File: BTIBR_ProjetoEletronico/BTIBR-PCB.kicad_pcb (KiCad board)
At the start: 2 copper layers, 100 x 100 mm, 63 parts, among them J1 Screw_Terminal_01x04, J10 Conn_01x03_Male, J11 Conn_01x03_Male, J12 Screw_Terminal_01x03, J13 Screw_Terminal_01x03, J14 Conn_01x03_Male, J15 Conn_01x03_Male, J16 Screw_Terminal_01x04, J17 Screw_Terminal_01x04, J18 Conn_01x03_Male, J19 Conn_01x03_Male, J2 Screw_Terminal_01x04, J20 Conn_01x03_Male, J21 Conn_01x03_Male, J22 Screw_Terminal_01x03, J23 Screw_Terminal_01x03, J3 Conn_01x03_Male, J4 Conn_01x03_Male, J5 Screw_Terminal_01x04, J6 Screw_Terminal_01x04, J7 Screw_Terminal_01x04, J8 Conn_01x03_Male, J9 Conn_01x03_Male, U1 PC817, U10 PC817, U11 DRV8825, U12 DRV8825, U13 PC817, U14 PC817, U15 PC817, U16 PC817, U17 PC817, U18 PC817, U19 PC817, U2 PC817, U20 PC817, U3 DRV8825, U4 DRV8825, U5 PC817, U6 PC817, U7 PC817, U8 PC817, U9 PC817

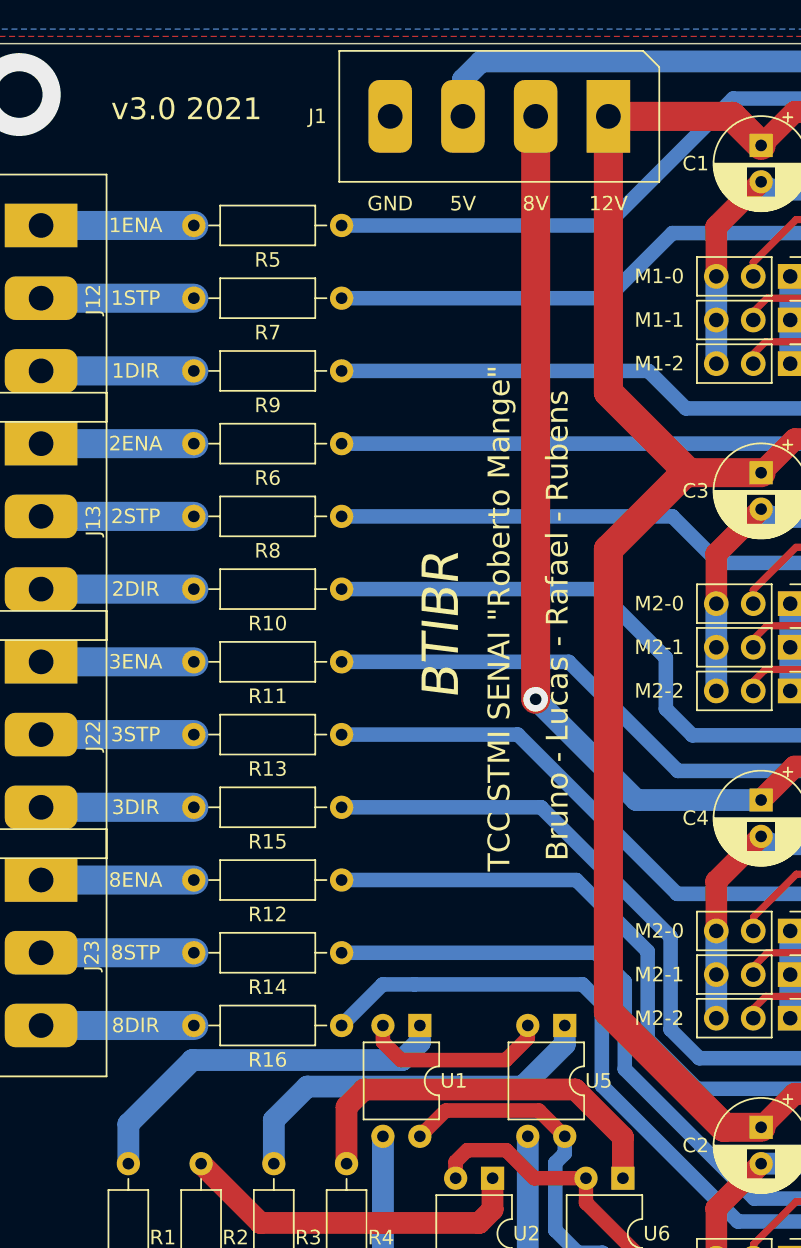
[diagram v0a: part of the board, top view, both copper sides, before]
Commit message: Adicionada PCB-1 (Arduino, LM2596 e MAX485)
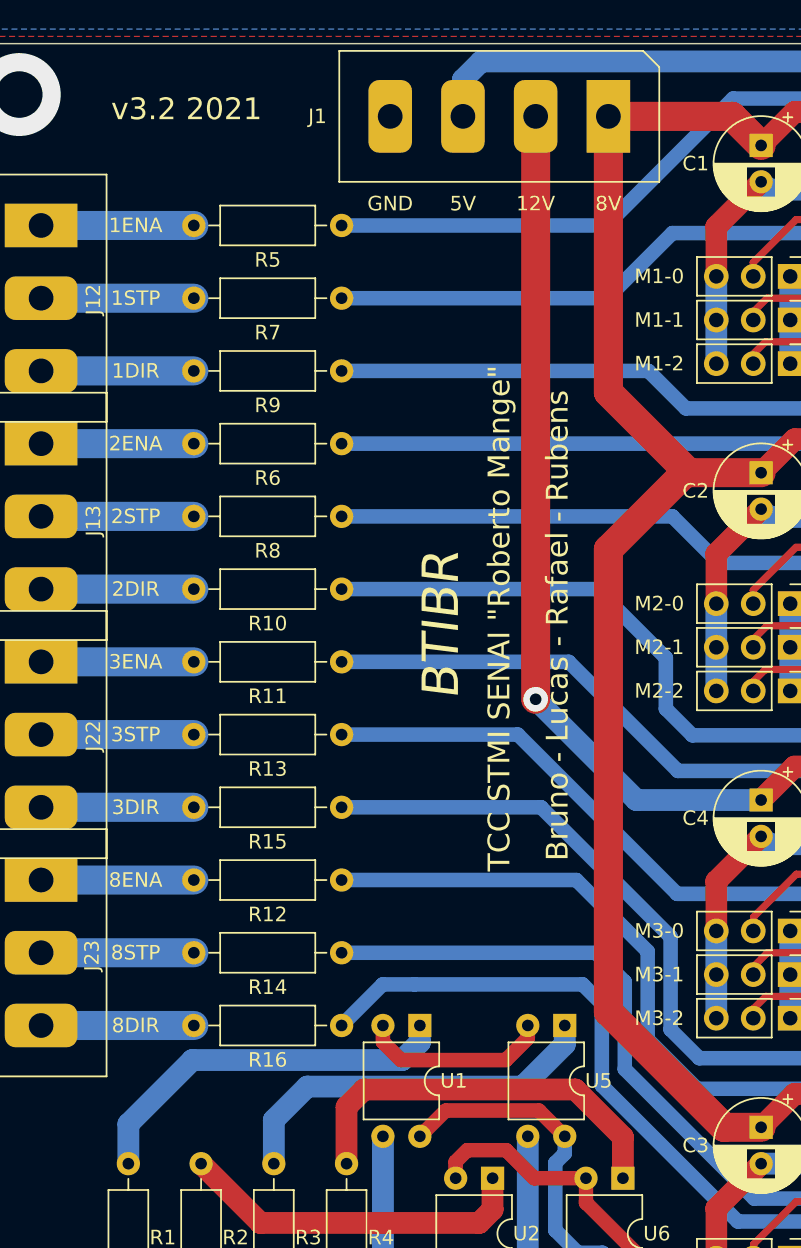
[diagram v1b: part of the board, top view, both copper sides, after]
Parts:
- moved C2 45.0 mm to (154.5, 79.5)
- moved C3 45.0 mm to (154.5, 124.5)
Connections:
- C1 pad 1: +12V -> +8V
- C2 pad 1: +12V -> +8V
- C3 pad 1: +12V -> +8V
- C4 pad 1: +8V -> +12V
- J1 pad 1: +12V -> +8V
- J1 pad 2: +8V -> +12V
- U11 pad 8: +8V -> +12V
- U12 pad 8: +12V -> +8V
- U3 pad 8: +12V -> +8V
- U4 pad 8: +12V -> +8V
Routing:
- net +8V: track 91.7 -> 196.2 mm, vias 1 -> 0
- net +12V: track 196.2 -> 91.7 mm, vias 0 -> 1
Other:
- board text added: "M3-0"
- board text added: "M3-1"
- board text added: "M3-2"
- board text added: "v3.2 2021"
- board text removed: "v3.0 2021"
